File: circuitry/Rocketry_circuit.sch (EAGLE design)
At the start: 7 parts

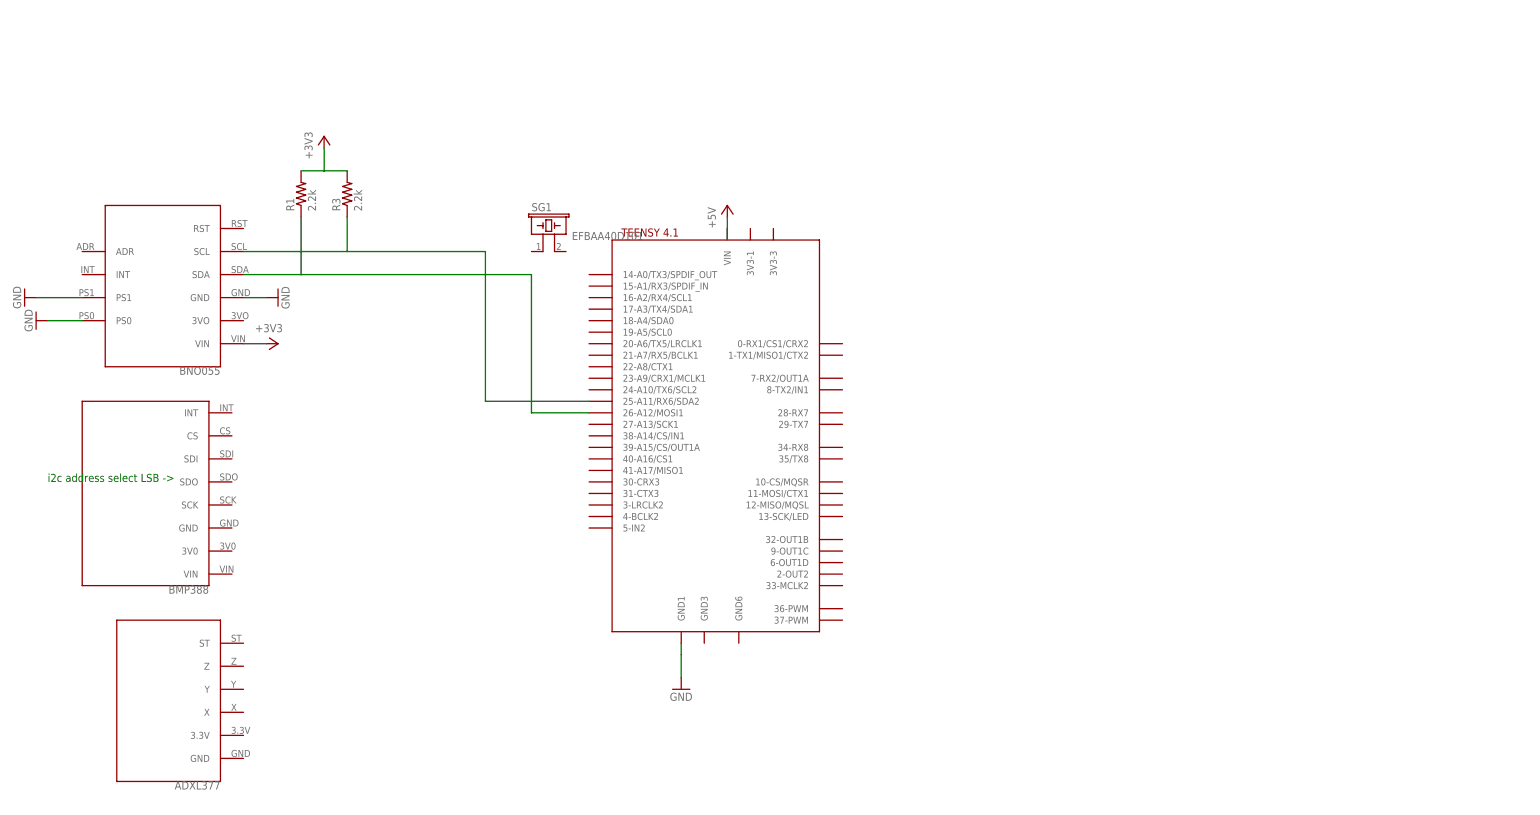
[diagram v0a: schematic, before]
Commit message: Added 3D files and proper footprints for all components, worked on brd design
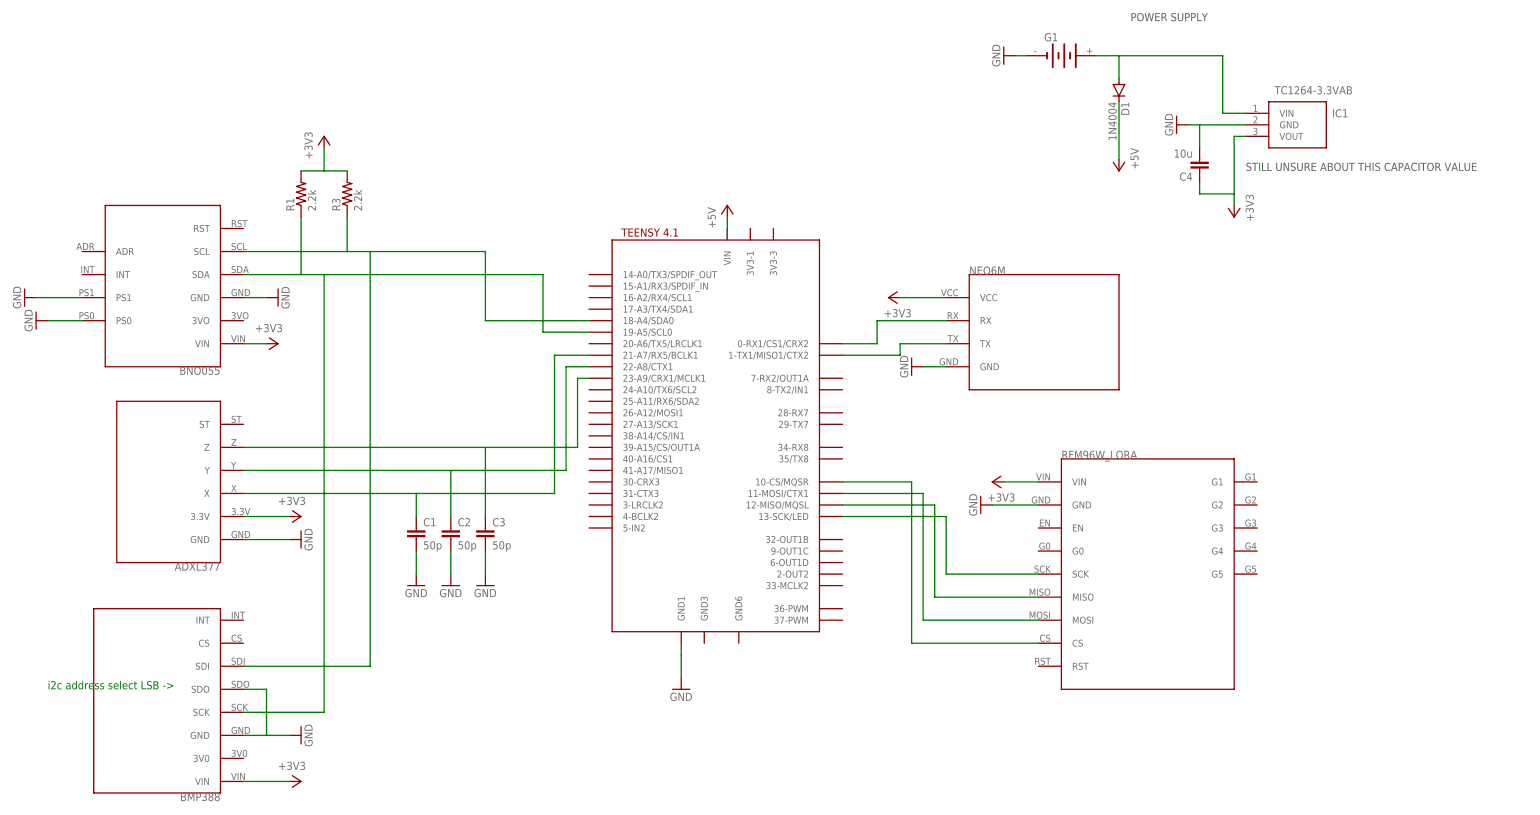
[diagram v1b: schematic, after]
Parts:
- removed SG1: EFBAA40D101, buzzer:EFBAA40D101
- added C1, C2, C3: 50p, capacitor-wima:C2,5-3
- added C4: 10u, capacitor-wima:C2,5-3
- added D1: 1N4004, diode:1N4004
- added G1: 3V11R, battery:3V11R
- added IC1: TC1264-3.3VAB, TC1264-3.3VAB:TC1264-3.3VAB
- added U$4: NEO6M, NEO6M:NEO6M
- added U$5: RFM96W, RMF96W_lora:RFM96W
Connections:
- new net N$1: C1.1, U$1.21-A7/RX5/BCLK1, U$3.X
- new net N$10: U$1.11-MOSI/CTX1, U$5.MOSI
- new net N$11: U$1.10-CS/MQSR, U$5.CS
- new net N$12: D1.A, G1.+, IC1.VIN
- new net N$2: C2.1, U$1.22-A8/CTX1, U$3.Y
- new net N$4: C3.1, U$1.23-A9/CRX1/MCLK1, U$3.Z
- new net N$6: U$1.0-RX1/CS1/CRX2, U$4.RX
- new net N$7: U$1.1-TX1/MISO1/CTX2, U$4.TX
- new net N$8: U$1.13-SCK/LED, U$5.SCK
- new net N$9: U$1.12-MISO/MQSL, U$5.MISO
- net +3V3: now also C4.1, IC1.VOUT, U$2.VIN, U$3.3.3V, U$4.VCC, U$5.VIN
- net +5V: now also D1.C
- net GND: now also C1.2, C2.2, C3.2, C4.2, G1.-, IC1.GND, U$2.GND, U$2.SDO, U$3.GND, U$4.GND, U$5.GND
- net N$3: now also U$1.19-A5/SCL0, U$2.SCK; no longer U$1.26-A12/MOSI1
- net N$5: now also U$1.18-A4/SDA0, U$2.SDI; no longer U$1.25-A11/RX6/SDA2
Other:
- note added: "POWER SUPPLY"
- note added: "STILL UNSURE ABOUT THIS CAPACITOR VALUE"

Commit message: power circuitry up to date
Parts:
- added C5: 100u, capacitor-wima:C2,5-3
- added D2: 1N4004, diode:1N4004
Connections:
- net +5V: now also D2.C
- net GND: now also C5.1
- net N$12: now also C5.2, D2.A
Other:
- moved on the sheet: C1, C2, C3, C4, D1, G1, IC1, R1, R3

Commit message: updated board size to 31.75mm width, to fit into 34mm transition shoulder section
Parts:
- U$2: value BMP388 -> BMP280; device BMP388:BMP388 -> BMP280:BMP280
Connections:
- net N$3: now also U$1.24-A10/TX6/SCL2
- net N$5: now also U$1.25-A11/RX6/SDA2
- net N$6: now also U$1.7-RX2/OUT1A
- net N$7: now also U$1.8-TX2/IN1
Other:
- note removed: "STILL UNSURE ABOUT THIS CAPACITOR VALUE"
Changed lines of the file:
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@@
 </layers>
 <schematic xreflabel="%F%N/%S.%C%R" xrefpart="/%S.%C%R">
+<fusionteam huburn="a.YnVzaW5lc3M6c2hlZmZpZWxkMjc4Nw" projecturn="a.YnVzaW5lc3M6c2hlZmZpZWxkMjc4NyMyMDIyMDMwMjUwMzA2NDc3Ng" folderUrn="urn:adsk.wipprod:fs.folder:co.I3GsyREKSyqqvbJB1hIioQ" urn="urn:adsk.wipprod:dm.lineage:APn9M5JCQH-6ql8Q4Hl2Ng"  versionUrn="urn:adsk.wipprod:fs.file:vf.APn9M5JCQH-6ql8Q4Hl2Ng?version=2" camFileUrn="" camFileVersionUrn="" lastpublishedchangeguid="3e0edd60-f172-4a0e-c01f-4f6dd1e2749d"/>
 <attributes>
 </attributes>
@@
 <part name="R3" library="adafruit" library_urn="urn:adsk.eagle:library:420" deviceset="R-US_" device="0207/5V" package3d_urn="urn:adsk.eagle:package:6240601/1" value="2.2k"/>
 <part name="R1" library="adafruit" library_urn="urn:adsk.eagle:library:420" deviceset="R-US_" device="0207/5V" package3d_urn="urn:adsk.eagle:package:6240601/1" value="2.2k"/>
-<part name="U$1" library="teensy" library_urn="urn:adsk.eagle:library:34376398" deviceset="TEENSY41" device="" package3d_urn="urn:adsk.eagle:package:34376405/4"/>
+<part name="U$1" library="teensy" library_urn="urn:adsk.eagle:library:34376398" deviceset="TEENSY41" device="" package3d_urn="urn:adsk.eagle:package:34376405/5"/>
 <part name="U$3" library="ADXL377" library_urn="urn:adsk.eagle:library:34388822" deviceset="ADXL377" device="" package3d_urn="urn:adsk.eagle:package:34388825/6"/>
 <part name="BRKOUT1" library="BNO055" library_urn="urn:adsk.eagle:library:34376417" deviceset="BNO055" device="" package3d_urn="urn:adsk.eagle:package:34376420/11"/>
@@
 <part name="+3V5" library="supply1" library_urn="urn:adsk.eagle:library:371" deviceset="+3V3" device=""/>
 <part name="GND6" library="supply1" library_urn="urn:adsk.eagle:library:371" deviceset="GND" device=""/>
-<part name="U$2" library="BMP388" library_urn="urn:adsk.eagle:library:34389065" deviceset="BMP388" device="" package3d_urn="urn:adsk.eagle:package:34389068/4"/>
 <part name="U$5" library="RMF96W_lora" library_urn="urn:adsk.eagle:library:34492806" deviceset="RFM96W" device="" package3d_urn="urn:adsk.eagle:package:34492839/4"/>
 <part name="+3V6" library="supply1" library_urn="urn:adsk.eagle:library:371" deviceset="+3V3" device=""/>
@@
 <part name="C5" library="capacitor-wima" library_urn="urn:adsk.eagle:library:116" deviceset="C" device="2,5-3" package3d_urn="urn:adsk.eagle:package:5436/1" value="100u"/>
 <part name="D2" library="diode" library_urn="urn:adsk.eagle:library:210" deviceset="1N4004" device="" package3d_urn="urn:adsk.eagle:package:43336/1"/>
+<part name="U$2" library="BMP280" library_urn="urn:adsk.eagle:library:34675788" deviceset="BMP280" device="" package3d_urn="urn:adsk.eagle:package:34675794/4"/>
 </parts>
 <sheets>
@@
 <text x="5.08" y="223.52" size="6.4516" layer="103">ONBOARD</text>
 <text x="274.32" y="213.36" size="1.778" layer="97">POWER SUPPLY</text>
-<text x="297.18" y="180.34" size="1.778" layer="97">STILL UNSURE ABOUT THIS CAPACITOR VALUE</text>
 </plain>
 <instances>
@@
 <attribute name="VALUE" x="86.36" y="48.26" size="1.778" layer="96"/>
 </instance>
-<instance part="GND4" gate="1" x="91.44" y="55.88" smashed="yes" rot="R90">
-<attribute name="VALUE" x="93.98" y="53.34" size="1.778" layer="96" rot="R90"/>
+<instance part="GND4" gate="1" x="96.52" y="55.88" smashed="yes" rot="R90">
+<attribute name="VALUE" x="99.06" y="53.34" size="1.778" layer="96" rot="R90"/>
 </instance>
 <instance part="U$4" gate="G$1" x="248.92" y="144.78" smashed="yes"/>
@@
 <attribute name="VALUE" x="223.52" y="139.7" size="1.778" layer="96" rot="R270"/>
 </instance>
-<instance part="U$2" gate="G$1" x="63.5" y="58.42" smashed="yes" rot="R180"/>
 <instance part="U$5" gate="G$1" x="259.08" y="66.04" smashed="yes"/>
 <instance part="+3V6" gate="G$1" x="243.84" y="111.76" smashed="yes" rot="R90">
@@
 <attribute name="VALUE" x="266.9286" y="195.58" size="1.778" layer="96" rot="R270"/>
 </instance>
+<instance part="U$2" gate="G$1" x="78.74" y="81.28" smashed="yes" rot="R180"/>
 </instances>
 <busses>
@@
 <pinref part="+3V3" gate="G$1" pin="+3V3"/>
 <wire x1="78.74" y1="104.14" x2="88.9" y2="104.14" width="0.1524" layer="91"/>
-</segment>
-<segment>
-<pinref part="+3V4" gate="G$1" pin="+3V3"/>
-<wire x1="78.74" y1="45.72" x2="88.9" y2="45.72" width="0.1524" layer="91"/>
-<pinref part="U$2" gate="G$1" pin="VIN"/>
 </segment>
 <segment>
@@
 <wire x1="289.56" y1="175.26" x2="297.18" y2="175.26" width="0.1524" layer="91"/>
 </segment>
+<segment>
+<pinref part="U$2" gate="G$1" pin="VIN"/>
+<pinref part="+3V4" gate="G$1" pin="+3V3"/>
+<wire x1="83.82" y1="45.72" x2="88.9" y2="45.72" width="0.1524" layer="91"/>
+</segment>
 </net>
 <net name="GND" class="0">
@@
 <pinref part="GND3" gate="1" pin="GND"/>
 <wire x1="78.74" y1="99.06" x2="88.9" y2="99.06" width="0.1524" layer="91"/>
-</segment>
-<segment>
-<pinref part="GND4" gate="1" pin="GND"/>
-<wire x1="88.9" y1="55.88" x2="83.82" y2="55.88" width="0.1524" layer="91"/>
-<wire x1="78.74" y1="66.04" x2="83.82" y2="66.04" width="0.1524" layer="91"/>
-<wire x1="83.82" y1="66.04" x2="83.82" y2="55.88" width="0.1524" layer="91"/>
-<pinref part="U$2" gate="G$1" pin="SDO"/>
-<pinref part="U$2" gate="G$1" pin="GND"/>
-<wire x1="83.82" y1="55.88" x2="78.74" y2="55.88" width="0.1524" layer="91"/>
 </segment>
 <segment>
@@
 <wire x1="289.56" y1="190.5" x2="299.72" y2="190.5" width="0.1524" layer="91"/>
 <wire x1="289.56" y1="187.96" x2="289.56" y2="190.5" width="0.1524" layer="91"/>
+</segment>
+<segment>
+<pinref part="GND4" gate="1" pin="GND"/>
+<pinref part="U$2" gate="G$1" pin="GND"/>
+<wire x1="93.98" y1="55.88" x2="88.9" y2="55.88" width="0.1524" layer="91"/>
+<pinref part="U$2" gate="G$1" pin="SDO"/>
+<wire x1="88.9" y1="55.88" x2="83.82" y2="55.88" width="0.1524" layer="91"/>
+<wire x1="83.82" y1="66.04" x2="88.9" y2="66.04" width="0.1524" layer="91"/>
+<wire x1="88.9" y1="66.04" x2="88.9" y2="55.88" width="0.1524" layer="91"/>
 </segment>
 </net>
@@
 <pinref part="U$1" gate="G$1" pin="19-A5/SCL0"/>
 <wire x1="144.78" y1="144.78" x2="154.94" y2="144.78" width="0.1524" layer="91"/>
-<wire x1="78.74" y1="60.96" x2="96.52" y2="60.96" width="0.1524" layer="91"/>
 <wire x1="96.52" y1="60.96" x2="96.52" y2="157.48" width="0.1524" layer="91"/>
+<wire x1="144.78" y1="144.78" x2="144.78" y2="132.08" width="0.1524" layer="91"/>
+<pinref part="U$1" gate="G$1" pin="24-A10/TX6/SCL2"/>
+<wire x1="144.78" y1="132.08" x2="154.94" y2="132.08" width="0.1524" layer="91"/>
 <pinref part="U$2" gate="G$1" pin="SCK"/>
+<wire x1="96.52" y1="60.96" x2="83.82" y2="60.96" width="0.1524" layer="91"/>
 </segment>
 </net>
@@
 <wire x1="106.68" y1="162.56" x2="132.08" y2="162.56" width="0.1524" layer="91"/>
 <wire x1="132.08" y1="162.56" x2="132.08" y2="147.32" width="0.1524" layer="91"/>
-<wire x1="132.08" y1="147.32" x2="154.94" y2="147.32" width="0.1524" layer="91"/>
-<wire x1="78.74" y1="71.12" x2="106.68" y2="71.12" width="0.1524" layer="91"/>
+<wire x1="132.08" y1="147.32" x2="142.24" y2="147.32" width="0.1524" layer="91"/>
+<wire x1="142.24" y1="147.32" x2="154.94" y2="147.32" width="0.1524" layer="91"/>
 <wire x1="106.68" y1="71.12" x2="106.68" y2="162.56" width="0.1524" layer="91"/>
+<pinref part="U$1" gate="G$1" pin="25-A11/RX6/SDA2"/>
+<wire x1="142.24" y1="147.32" x2="142.24" y2="129.54" width="0.1524" layer="91"/>
+<wire x1="142.24" y1="129.54" x2="154.94" y2="129.54" width="0.1524" layer="91"/>
 <pinref part="U$2" gate="G$1" pin="SDI"/>
+<wire x1="83.82" y1="71.12" x2="106.68" y2="71.12" width="0.1524" layer="91"/>
 </segment>
 </net>
@@
 <wire x1="218.44" y1="147.32" x2="218.44" y2="142.24" width="0.1524" layer="91"/>
 <pinref part="U$1" gate="G$1" pin="0-RX1/CS1/CRX2"/>
-<wire x1="218.44" y1="142.24" x2="210.82" y2="142.24" width="0.1524" layer="91"/>
+<wire x1="218.44" y1="142.24" x2="213.36" y2="142.24" width="0.1524" layer="91"/>
+<wire x1="213.36" y1="142.24" x2="210.82" y2="142.24" width="0.1524" layer="91"/>
+<wire x1="213.36" y1="142.24" x2="213.36" y2="134.62" width="0.1524" layer="91"/>
+<pinref part="U$1" gate="G$1" pin="7-RX2/OUT1A"/>
+<wire x1="213.36" y1="134.62" x2="210.82" y2="134.62" width="0.1524" layer="91"/>
 </segment>
 </net>
@@
 <segment>
 <pinref part="U$1" gate="G$1" pin="1-TX1/MISO1/CTX2"/>
-<wire x1="210.82" y1="139.7" x2="223.52" y2="139.7" width="0.1524" layer="91"/>
+<wire x1="210.82" y1="139.7" x2="215.9" y2="139.7" width="0.1524" layer="91"/>
+<wire x1="215.9" y1="139.7" x2="223.52" y2="139.7" width="0.1524" layer="91"/>
 <wire x1="223.52" y1="139.7" x2="223.52" y2="142.24" width="0.1524" layer="91"/>
 <pinref part="U$4" gate="G$1" pin="TX"/>
 <wire x1="223.52" y1="142.24" x2="233.68" y2="142.24" width="0.1524" layer="91"/>
-</segment>
-</net>
+<wire x1="215.9" y1="139.7" x2="215.9" y2="132.08" width="0.1524" layer="91"/>
+<pinref part="U$1" gate="G$1" pin="8-TX2/IN1"/>
+<wire x1="215.9" y1="132.08" x2="210.82" y2="132.08" width="0.1524" layer="91"/>
+</segment>
+</net>
